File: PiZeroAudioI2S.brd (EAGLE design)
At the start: 65.1 x 30.2 mm, 69 parts, among them CON1 RPI-Header, J1 GROVE, J2 2X2HEADER, J3 2X1-LOCKING, J4 GROVE, J5 4X1-LOCKING, Q1 DMG2305UX, U1 TXB0104PWR, U2 LSM6DS33, U3 PCM5101A, U4 DMMT5401, U5 TXS0102, U6 TPA3144D2PWPR

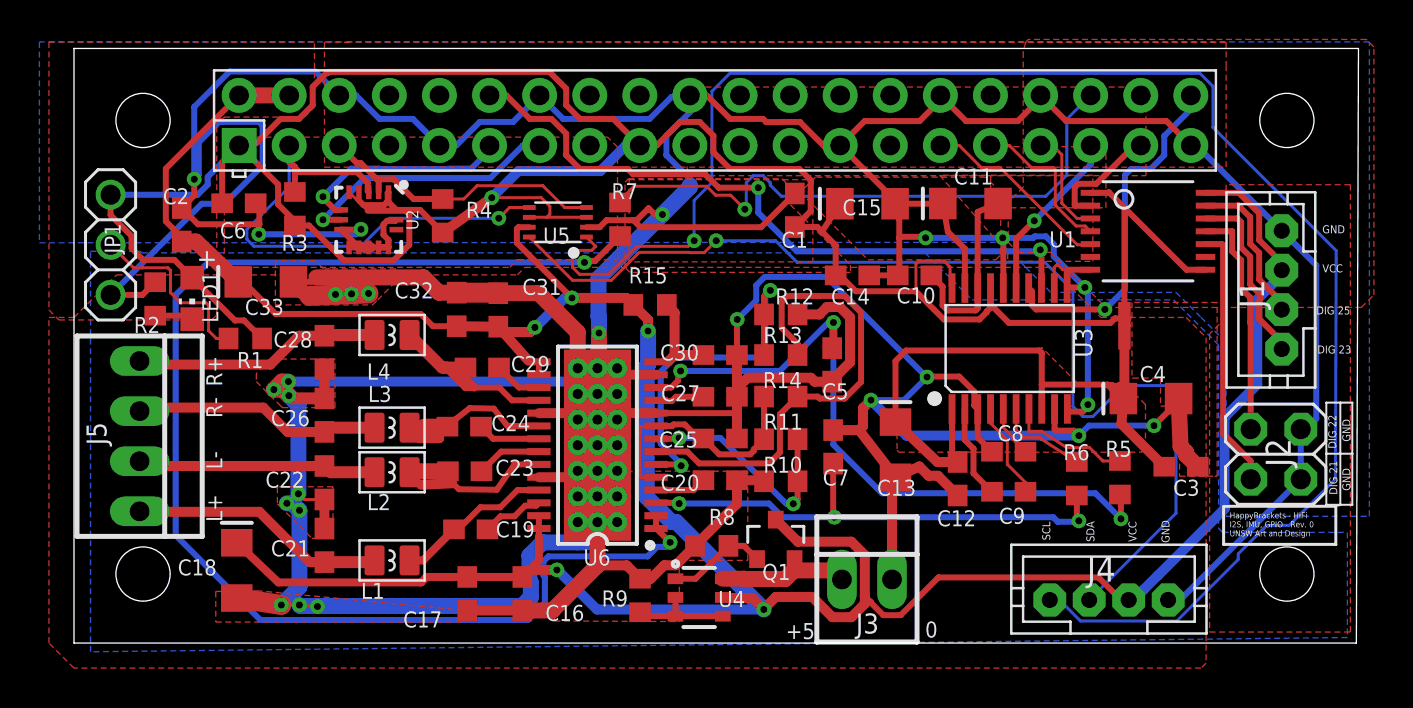
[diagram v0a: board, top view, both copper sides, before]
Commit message: Swapped position of Mosfet Capacitively coupled Audio Set OE of I2C translator to GND Set Mute so it floats to +5
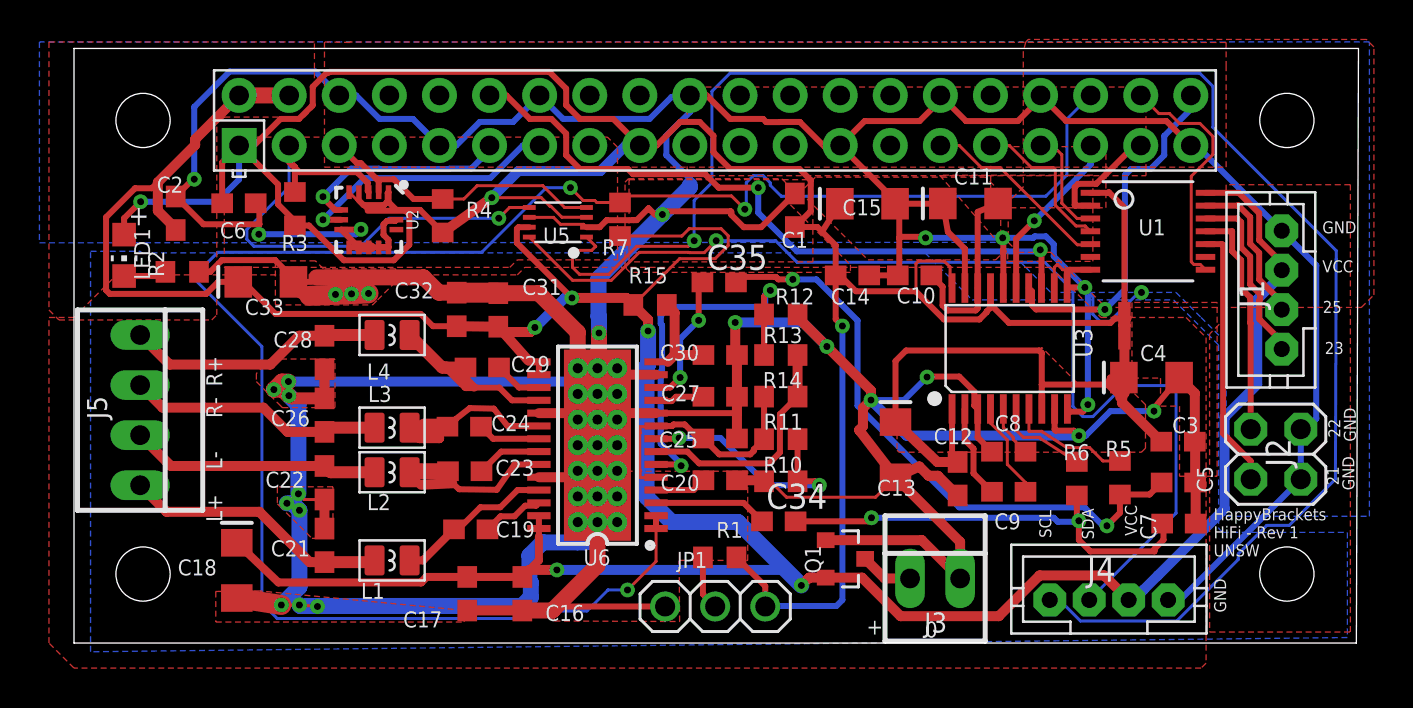
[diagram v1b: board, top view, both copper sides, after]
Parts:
- removed R8: 47K, adafruit:R0603
- removed R9: 10K, adafruit:R0603
- removed U4: DMMT5401, HappyBrackets:SOT26-TRANS
- added C34, C35: 1uF, rcl:C0603
- moved JP1 35.7 mm to (-46.2, 3.12), turned to 180 degrees
- moved R1 26.5 mm to (-46.0, 5.61)
- moved C5 18.5 mm to (-22.7, 9.41), turned to 0 degrees
- moved C7 18.0 mm to (-22.7, 7.33), turned to 0 degrees
- moved LED1 4.09 mm to (-76.2, 20.9)
- moved Q1 3.67 mm to (-39.6, 5.54), turned to 270 degrees
- moved J3 3.45 mm to (-35.1, 4.55)
- moved R2 1.94 mm to (-73.3, 20.1), turned to 180 degrees
- moved J5 1.32 mm to (-75.4, 13.1)
- moved C3 1.28 mm to (-22.8, 11.5)
- moved C4 1.07 mm to (-24.1, 14.7)
- moved C2 0.66 mm to (-73.6, 23.1)
- turned R7 to 90 degrees
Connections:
- removed net N$22: R9.1, U4.B1, U4.B2, U4.C2
- removed net N$27: Q1.G, R8.1, U4.C1
- removed net N$5: R7.2, U6.1, U6.2
- new net N$14: C34.1, U6.3
- new net N$15: C35.1, U6.12
- new net OE: CON1.38, U1.8
- net +3V3: no longer U1.8, U5.P$6
- net +5V: now also Q1.S, R7.1; no longer Q1.D, U4.E2
- net +5V-IN: now also Q1.D; no longer Q1.S, U4.E1
- net /MUTE: now also R7.2, U6.1, U6.2; no longer R7.1
- net AGND: now also JP1.3, Q1.G, R2.1; no longer R8.2, R9.2
- net AUDIO-LEFT: now also C34.2; no longer U6.3
- net AUDIO-RIGHT: now also C35.2; no longer U6.12
- net GND: now also U5.P$6; no longer JP1.3, R2.1
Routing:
- net N$5: track 67.5 -> 0.00 mm, vias 2 -> 0
- net /MUTE: track 30.5 -> 96.0 mm, vias 1 -> 3
- net GND: track 205.5 -> 191.6 mm, vias 9 -> 10
- net +5V: track 154.1 -> 166.8 mm
- net N$24: track 24.6 -> 12.1 mm
- net OE: track 0.00 -> 12.2 mm
- net N$15: track 0.00 -> 6.72 mm, vias 0 -> 2
- net +3V3: track 143.4 -> 150.0 mm, vias 1 -> 3
- net PWR-LED: track 9.36 -> 2.75 mm
- net N$14: track 0.00 -> 5.76 mm
- net N$22: track 5.23 -> 0.00 mm
- net N$27: track 5.10 -> 0.00 mm
- net AUDIO-RIGHT: track 35.5 -> 30.9 mm, vias 3 -> 2
- net +5V-IN: track 7.00 -> 2.69 mm
- net AUDIO-LEFT: track 25.9 -> 22.5 mm, vias 3 -> 2
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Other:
- board text added: "+"
- board text added: "21"
- board text added: "22"
- board text added: "23"
- board text added: "25"
- board text added: "HappyBrackets HiFi - Rev 1 UNSW"
- board text removed: "+5"
- board text removed: "DIG 21"
- board text removed: "DIG 22"
- board text removed: "DIG 23"
- board text removed: "DIG 25"
- board text removed: "HappyBrackets - HiFi I2S, IMU, GPIO - Rev. 0 UNSW Art and Design"

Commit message: Adjusted Layout
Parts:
- moved C7 5.03 mm to (-27.0, 9.90), turned to 90 degrees
- moved R6 1.25 mm to (-29.1, 9.86)
- moved R5 0.76 mm to (-25.0, 9.91)
- moved C3 0.48 mm to (-22.3, 11.5)
- moved C5 0.46 mm to (-22.3, 9.36)
- moved C9 0.35 mm to (-31.7, 8.84)
- moved C8 0.33 mm to (-31.7, 10.9)
- moved C12 0.25 mm to (-34.2, 9.60)
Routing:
- net AGND: track 269.2 -> 276.1 mm
- net AUDIO-LEFT: track 22.5 -> 18.5 mm
- net N$11: track 4.68 -> 3.71 mm
- net N$1: track 6.26 -> 6.96 mm
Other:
- board text added: "-"
- board text removed: "0"

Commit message: Build Revision 1
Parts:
- removed R14: 33K, adafruit:R0603
- removed R15: 10R, adafruit:R0603
- removed U6: TPA3144D2PWPR, HappyBrackets:HTSSOP28
- added R8: 39K, adafruit:R0603
- added R9: 56K, adafruit:R0603
- added U4: TXS0102, adafruit:VFSOP-8
- C19: value 220nF -> 1uF
- C20, C25: value 1uF -> 220nF
- C21, C26, C28: value 1nF -> 1uF
- C23, C29: value 220nF -> 1nF
- C27: value 1uF -> 1nF
- C31: value 1nF -> 220nF
- C32: value 0.1uF -> 1uF
- C33: value 100uF -> 1nF; device HappyBrackets:EIA3216 -> rcl:C0603
- C34: value 1uF -> 0.1uF
- C35: value 1uF -> 100uF; device rcl:C0603 -> HappyBrackets:EIA3216
- R10: value 39K -> 33K
- R11: value 56K -> 33K
- R13: value 33K -> 10R
- R5, R6: value 470 -> 80K
- U5: value TXS0102 -> TPA3144D2PWPR; device adafruit:VFSOP-8 -> HappyBrackets:HTSSOP28
- moved C35 23.0 mm to (-69.0, 19.6), turned to 180 degrees
- moved C21 20.3 mm to (-46.0, 9.53), turned to 0 degrees
- moved C28 20.2 mm to (-46.0, 13.8), turned to 0 degrees
- moved C26 20.1 mm to (-46.0, 11.6), turned to 0 degrees
- moved C27 20.1 mm to (-66.0, 12.8), turned to 90 degrees
- moved C34 19.5 mm to (-59.3, 18.2), turned to 90 degrees
- moved C19 15.6 mm to (-43.0, 7.44)
- moved C32 13.6 mm to (-46.0, 15.9), turned to 0 degrees
- moved C25 13.0 mm to (-59.0, 12.2)
- moved C20 12.9 mm to (-58.6, 7.04)
- moved C33 11.9 mm to (-57.2, 18.2), turned to 90 degrees
- moved U5 11.5 mm to (-52.2, 11.3)
- moved R10 8.46 mm to (-42.9, 17.9), turned to 0 degrees
- moved C29 8.04 mm to (-66.0, 16.0), turned to 90 degrees
- moved C23 7.14 mm to (-66.0, 9.40), turned to 90 degrees
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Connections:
- net +3V3: now also U4.P$3; no longer U5.P$3
- net +5V: now also C33.1, C34.1, C35.+, R13.2, U4.P$7, U5.15, U5.16, U5.27, U5.28; no longer C31.1, C32.1, C33.+, R15.2, U5.P$7, U6.15, U6.16, U6.27, U6.28
- net /MUTE: now also U5.1, U5.2; no longer U6.1, U6.2
- net AGND: now also C22.2, C23.1, C28.2, C29.1, C33.2, C34.2, C35.-, R8.2, U5.10, U5.13, U5.19, U5.24, U5.GND@10, U5.GND@11, U5.GND@12, U5.GND@13, U5.GND@14, U5.GND@15, U5.GND@16, U5.GND@17, U5.GND@18, U5.GND@19, U5.GND@20, U5.GND@21, U5.GND@22, U5.GND@23, U5.GND@24, U5.GND@25, U5.GND@26, U5.GND@27, U5.GND@28, U5.GND@29, U5.GND@30, U5.GND@PAD; no longer C20.2, C22.1, C25.2, C28.1, C30.2, C31.2, C33.-, R12.2, U6.10, U6.13, U6.19, U6.24, U6.GND@10, U6.GND@11, U6.GND@12, U6.GND@13, U6.GND@14, U6.GND@15, U6.GND@16, U6.GND@17, U6.GND@18, U6.GND@19, U6.GND@20, U6.GND@21, U6.GND@22, U6.GND@23, U6.GND@24, U6.GND@25, U6.GND@26, U6.GND@27, U6.GND@28, U6.GND@29, U6.GND@30, U6.GND@PAD
- net AUDIO-LEFT: now also C19.2; no longer C34.2
- net AUDIO-RIGHT: now also C30.2; no longer C35.2
- net GND: now also U4.P$2, U4.P$6; no longer U5.P$2, U5.P$6
- net L+: now also C22.1; no longer C21.1
- net L-: now also C23.2; no longer C22.2
- net N$10: now also C31.2, U5.17; no longer C29.2, U6.17
- net N$13: now also C25.2, U5.21; no longer C24.2, U6.21
- net N$14: now also C19.1, U5.3; no longer C34.1, U6.3
- net N$15: now also C30.1, U5.12; no longer C35.1, U6.12
- net N$16: now also C24.2, U5.22; no longer C23.2, U6.22
- net N$17: now also C20.2, U5.26; no longer C19.2, U6.26
- net N$18: now also C20.1, U5.25; no longer C19.1, U6.25
- net N$19: now also C24.1, U5.23; no longer C23.1, U6.23
- net N$20: now also C25.1, U5.20; no longer C24.1, U6.20
- net N$21: now also C31.1, U5.18; no longer C29.1, U6.18
- net N$23: now also R10.1, R11.2, U5.6; no longer R12.1, R13.2, U6.6
- net N$24: now also R11.1, R12.2, U5.7; no longer R13.1, R14.2, U6.7
- net N$25: now also R8.1, R9.2, U5.8; no longer R10.1, R11.2, U6.8
- net N$26: now also C26.1, R12.1, R9.1, U5.5, U5.9; no longer C25.1, R11.1, R14.1, U6.5, U6.9
- net N$7: now also C21.1, U5.4; no longer C20.1, U6.4
- net N$8: now also C28.1, U5.11; no longer C27.1, U6.11
- net N$9: now also C32.1, R13.1, U5.14; no longer C30.1, R15.1, U6.14
- net R+: now also C29.2; no longer C28.2
- net R-: now also C27.1; no longer C26.1
- net SCL: now also U4.P$4; no longer U5.P$4
- net SCL-OUT: now also U4.P$1; no longer U5.P$1
- net SDA: now also U4.P$5; no longer U5.P$5
- net SDA-OUT: now also U4.P$8; no longer U5.P$8
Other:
- board size 65.1 x 30.2 mm -> 65.3 x 30.3 mm

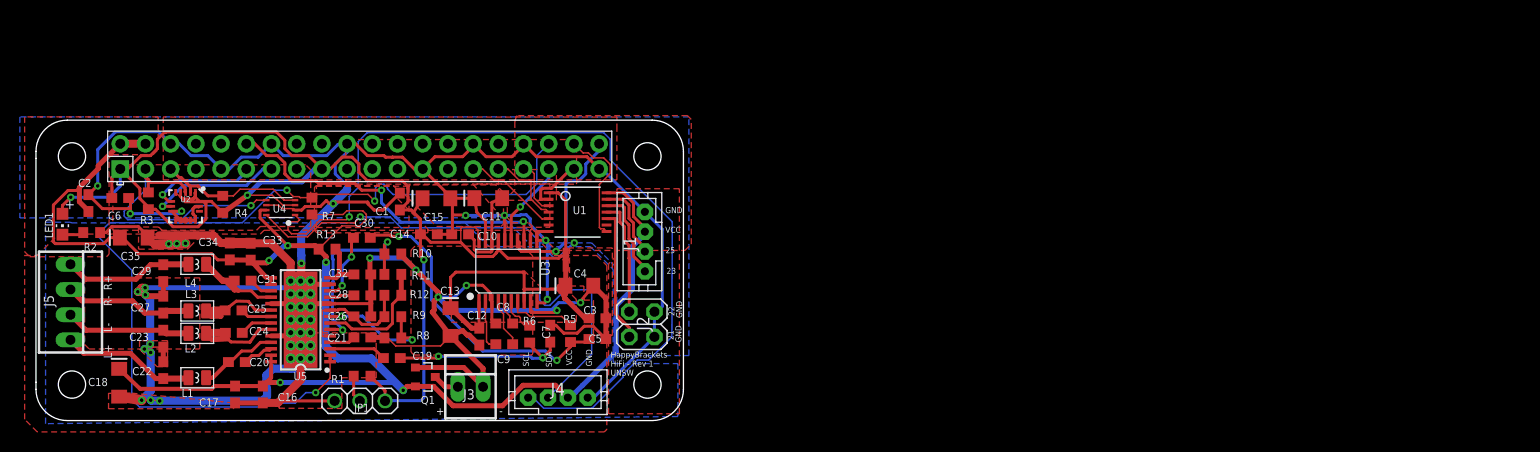
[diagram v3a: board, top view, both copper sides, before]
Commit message: Added R14 10K resistance to translator
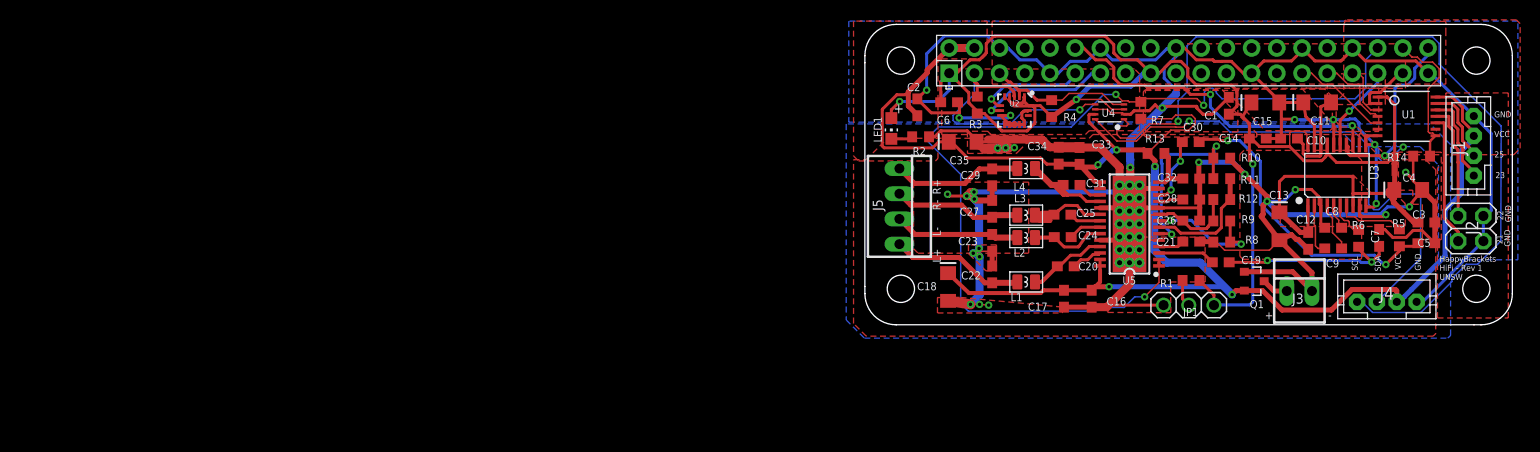
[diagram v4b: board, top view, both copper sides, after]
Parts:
- added R14: 10K, adafruit:R0603
- R5, R6: value 80K -> 76K8
- moved C12 84.1 mm to (49.4, 19.3)
- moved C13 84.1 mm to (46.5, 20.7)
- moved C19 84.1 mm to (40.5, 17.1)
- moved C22 84.1 mm to (17.5, 15.9)
- moved C23 84.1 mm to (17.5, 19.1)
- moved C27 84.1 mm to (17.5, 22.5)
- moved C29 84.1 mm to (17.5, 25.7)
- moved C6 84.1 mm to (13.2, 33.2)
- moved J1 84.1 mm to (66.0, 28.8)
- moved J2 84.1 mm to (65.7, 18.0)
- moved J5 84.1 mm to (8.15, 22.7)
- moved JP1 84.1 mm to (37.3, 12.8)
- moved Q1 84.1 mm to (43.9, 15.2)
- moved R1 84.1 mm to (37.5, 15.3)
- moved R2 84.1 mm to (10.3, 29.7)
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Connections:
- net AGND: now also R14.1
- net OE: now also R14.2
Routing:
- net AGND: track 276.1 -> 240.2 mm, vias 18 -> 20
- net N$19: track 10.5 -> 7.71 mm
- net OE: track 12.2 -> 14.5 mm
- net +5V: track 166.8 -> 167.4 mm
- added copper zone on layer 16, net AGND
- removed copper zone on layer 16, net ANGND

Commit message: Update for Move account
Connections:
- net +3V3: now also U4.P$6
- net GND: now also C11.-; no longer C11.+, U4.P$6
- net N$12: now also C11.+; no longer C11.-
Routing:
- net N$12: track 9.70 -> 0.00 mm
- net GND: track 191.6 -> 186.2 mm
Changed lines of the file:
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@@
 <?xml version="1.0" encoding="utf-8"?>
 <!DOCTYPE eagle SYSTEM "eagle.dtd">
-<eagle version="9.1.3">
+<eagle version="9.4.1">
 <drawing>
 <settings>
@@
 <contactref element="C10" pad="2"/>
 <contactref element="C14" pad="1"/>
-<contactref element="C15" pad="-"/>
-<contactref element="C11" pad="+"/>
-<contactref element="U3" pad="19"/>
 <contactref element="U3" pad="10"/>
 <contactref element="U3" pad="11"/>
@@
 <wire x1="55.1434" y1="29.718" x2="55.1578" y2="29.7036" width="0.3048" layer="1"/>
 <wire x1="55.1578" y1="29.7036" x2="55.1578" y2="28.9222" width="0.3048" layer="1"/>
-<wire x1="46.6462" y1="33.276125" x2="46.4342" y2="33.1978" width="0.3048" layer="1"/>
 <wire x1="46.6462" y1="33.276125" x2="46.6462" y2="33.1564" width="0.3048" layer="1"/>
 <wire x1="46.6462" y1="29.64" x2="46.5718" y2="29.5656" width="0.3048" layer="1"/>
 <wire x1="46.5718" y1="29.5656" x2="45.1222" y2="29.5656" width="0.3048" layer="1"/>
-<wire x1="46.4342" y1="33.1978" x2="48.8452625" y2="33.1978" width="0.3048" layer="1"/>
-<wire x1="48.85669375" y1="33.20923125" x2="49.109609375" y2="31.779115625" width="0.3048" layer="1"/>
-<wire x1="49.109609375" y1="31.779115625" x2="49.9728" y2="30.915925" width="0.3048" layer="1"/>
-<wire x1="49.9728" y1="30.915925" x2="49.9728" y2="28.9222" width="0.3048" layer="1"/>
 <wire x1="55.1728" y1="22.7922" x2="55.3082" y2="22.6568" width="0.3048" layer="1"/>
 <wire x1="55.3082" y1="22.6568" x2="55.9562" y2="22.6568" width="0.3048" layer="1"/>
@@
 <wire x1="46.6462" y1="33.1564" x2="46.6462" y2="31.4706" width="0.3048" layer="1"/>
 <wire x1="46.6462" y1="31.4706" x2="46.6462" y2="29.64" width="0.3048" layer="1"/>
-<wire x1="48.8452625" y1="33.1978" x2="48.85669375" y2="33.20923125" width="0.3048" layer="1"/>
 <wire x1="46.6462" y1="31.4706" x2="46.697" y2="31.5214" width="0.3048" layer="1"/>
 <wire x1="47.927003125" y1="31.5214" x2="47.9806" y2="31.467803125" width="0.3048" layer="1"/>
@@
 <wire x1="54.6608" y1="30.1244" x2="54.9344" y2="29.8508" width="0.1524" layer="1"/>
 <wire x1="54.9344" y1="29.8508" x2="55.2762" y2="29.8508" width="0.1524" layer="1"/>
-<contactref element="U4" pad="P$6"/>
 <wire x1="30.6406" y1="32.1544" x2="30.787" y2="32.008" width="0.1524" layer="1"/>
 <wire x1="29.46674375" y1="32.1544" x2="29.11314375" y2="32.508" width="0.1524" layer="1"/>
@@
 <wire x1="56.467" y1="27.58705" x2="56.467" y2="28.496" width="0.1524" layer="16"/>
 <wire x1="56.467" y1="28.496" x2="56.0578" y2="28.9052" width="0.1524" layer="16"/>
-<wire x1="29.11314375" y1="32.508" x2="27.887" y2="32.508" width="0.1524" layer="1"/>
 <wire x1="10.8966" y1="34.4424" x2="10.834" y2="34.4424" width="0.3048" layer="1"/>
 <wire x1="38.131" y1="32.6354875" x2="38.131" y2="32.7858" width="0.3048" layer="1"/>
@@
 <wire x1="34.798" y1="32.8168" x2="34.6329" y2="32.6517" width="0.3048" layer="1"/>
 <wire x1="12.66850625" y1="39.8782" x2="17.0644" y2="39.8782" width="0.254" layer="16"/>
+<contactref element="C11" pad="-"/>
+<contactref element="U3" pad="19"/>
+<wire x1="49.109609375" y1="31.779115625" x2="49.9728" y2="30.915925" width="0.3048" layer="1"/>
+<wire x1="49.9728" y1="30.915925" x2="49.9728" y2="28.9222" width="0.3048" layer="1"/>
+<contactref element="C15" pad="-"/>
+<wire x1="51.8898" y1="31.4678" x2="51.65669375" y2="33.20923125" width="0" layer="19" extent="1-1"/>
+<wire x1="46.4342" y1="33.1978" x2="46.6462" y2="33.276125" width="0" layer="19" extent="1-1"/>
+<wire x1="49.109609375" y1="31.779115625" x2="47.9806" y2="31.467803125" width="0" layer="19" extent="1-16"/>
 </signal>
 <signal name="PCM_FS">
@@
 <wire x1="39.8526" y1="12.7762" x2="39.8526" y2="13.804" width="0.3048" layer="1"/>
 <wire x1="39.8526" y1="13.804" x2="38.3912" y2="15.2654" width="0.3048" layer="1"/>
+<contactref element="U4" pad="P$6"/>
+<wire x1="28.496" y1="33.5054" x2="27.887" y2="32.508" width="0" layer="19" extent="1-1"/>
 </signal>
 <signal name="SDA">
@@
 <wire x1="50.0808" y1="18.7532" x2="50.3428" y2="18.4912" width="0.1524" layer="1"/>
 </signal>
-<signal name="N$12">
-<contactref element="U3" pad="18"/>
-<contactref element="C11" pad="-"/>
-<contactref element="C10" pad="1"/>
-<wire x1="50.6228" y1="28.9222" x2="50.6228" y2="32.785271875" width="0.3048" layer="1"/>
-<wire x1="50.6228" y1="32.785271875" x2="51.65669375" y2="33.20923125" width="0.3048" layer="1"/>
-<wire x1="48.2718" y1="29.5656" x2="48.843" y2="28.9944" width="0.3048" layer="1"/>
-<wire x1="48.843" y1="28.9944" x2="48.843" y2="28.04595" width="0.3048" layer="1"/>
-<wire x1="48.843" y1="28.04595" x2="49.10135" y2="27.7876" width="0.3048" layer="1"/>
-<wire x1="49.10135" y1="27.7876" x2="50.5206" y2="27.7876" width="0.3048" layer="1"/>
-<wire x1="50.5206" y1="27.7876" x2="50.6228" y2="27.8898" width="0.3048" layer="1"/>
-<wire x1="50.6228" y1="27.8898" x2="50.6228" y2="28.9222" width="0.3048" layer="1"/>
-</signal>
 <signal name="N$11">
 <contactref element="U3" pad="6"/>
@@
 <wire x1="35.0306" y1="23.88" x2="34.3136" y2="23.88" width="0.3048" layer="1"/>
 </signal>
+<signal name="N$12">
+<contactref element="U3" pad="18"/>
+<contactref element="C11" pad="+"/>
+<contactref element="C10" pad="1"/>
+<wire x1="48.2718" y1="29.5656" x2="48.85669375" y2="33.20923125" width="0" layer="19" extent="1-1"/>
+<wire x1="50.6228" y1="28.9222" x2="48.2718" y2="29.5656" width="0" layer="19" extent="1-1"/>
+</signal>
 </signals>
